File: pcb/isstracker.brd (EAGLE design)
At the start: 68.6 x 54.3 mm, 20 parts, among them IC2 L7805CV, J1 MOTOR_RIGHT, J3 MOTOR_LEFT, J4 DISPLAY, J5 CONTROL, J8 UART, J9 DISTANCE, U1 ARGON, X1 +12V

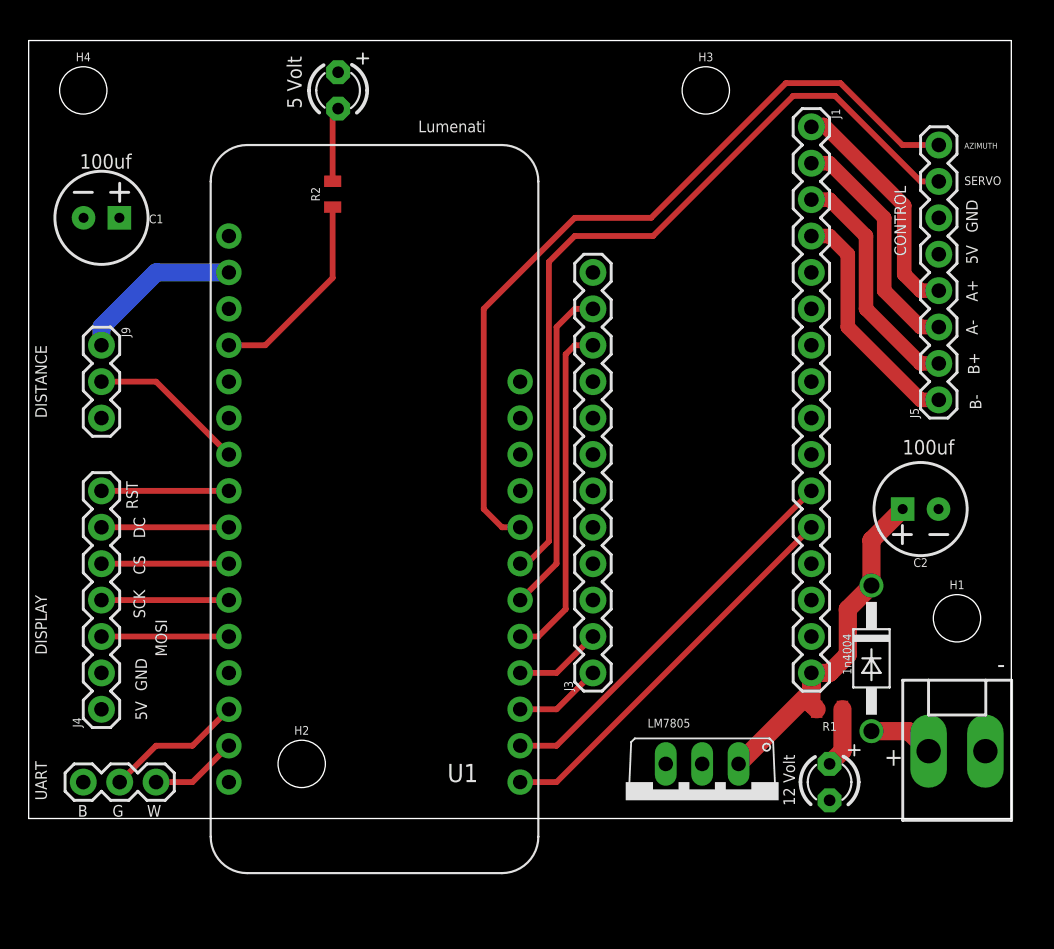
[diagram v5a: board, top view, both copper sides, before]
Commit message: PCB fixups
* Bumped PCB revisions
* Layout changes and some silk screen updates
* No functionality changes
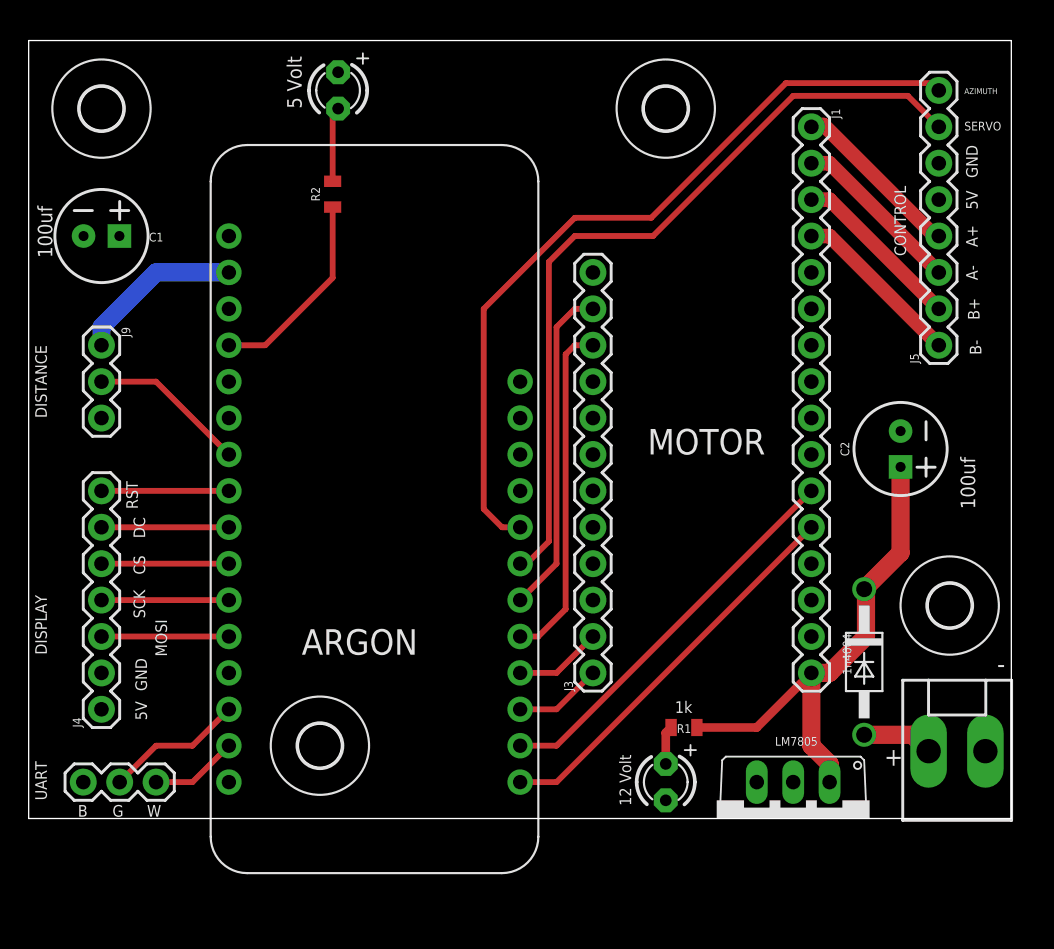
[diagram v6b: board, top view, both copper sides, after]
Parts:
- H1, H2, H3, H4: value STAND-OFF -> MOUNT-HOLE3.0; device SparkFun-Hardware:STAND-OFF -> holes:3,0
- moved H2 46.5 mm to (64.3, 14.9)
- moved H1 45.3 mm to (20.3, 5.08)
- moved LED1 11.4 mm to (44.5, 2.54)
- moved R1 10.2 mm to (45.7, 6.35), turned to 0 degrees
- moved IC2 6.48 mm to (53.3, 0.00)
- moved C2 4.42 mm to (60.8, 25.8), turned to 270 degrees
- moved J5 3.81 mm to (63.5, 33.0)
- moved H3 3.07 mm to (44.5, 49.5)
- moved H4 1.80 mm to (5.08, 49.5)
- moved C1 1.27 mm to (5.08, 40.6)
- moved D1 0.57 mm to (58.3, 10.9)
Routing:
- net +12V: track 26.0 -> 35.5 mm
- net B-: track 16.6 -> 12.0 mm
- net B+: track 16.6 -> 12.0 mm
- net A-: track 16.6 -> 12.0 mm
- net A+: track 16.5 -> 12.2 mm
- net SERVO: track 56.6 -> 55.0 mm
- net AZIMUTH: track 57.1 -> 55.5 mm
- net N$2: track 4.18 -> 2.69 mm
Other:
- board text added: "1k"
- board text added: "ARGON"
- board text added: "MOTOR"
- board text removed: "Lumenati"

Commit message: Fixups
* Add the ability to turn the power to the globe on and off via a MOSFET
* Clean up some of the code
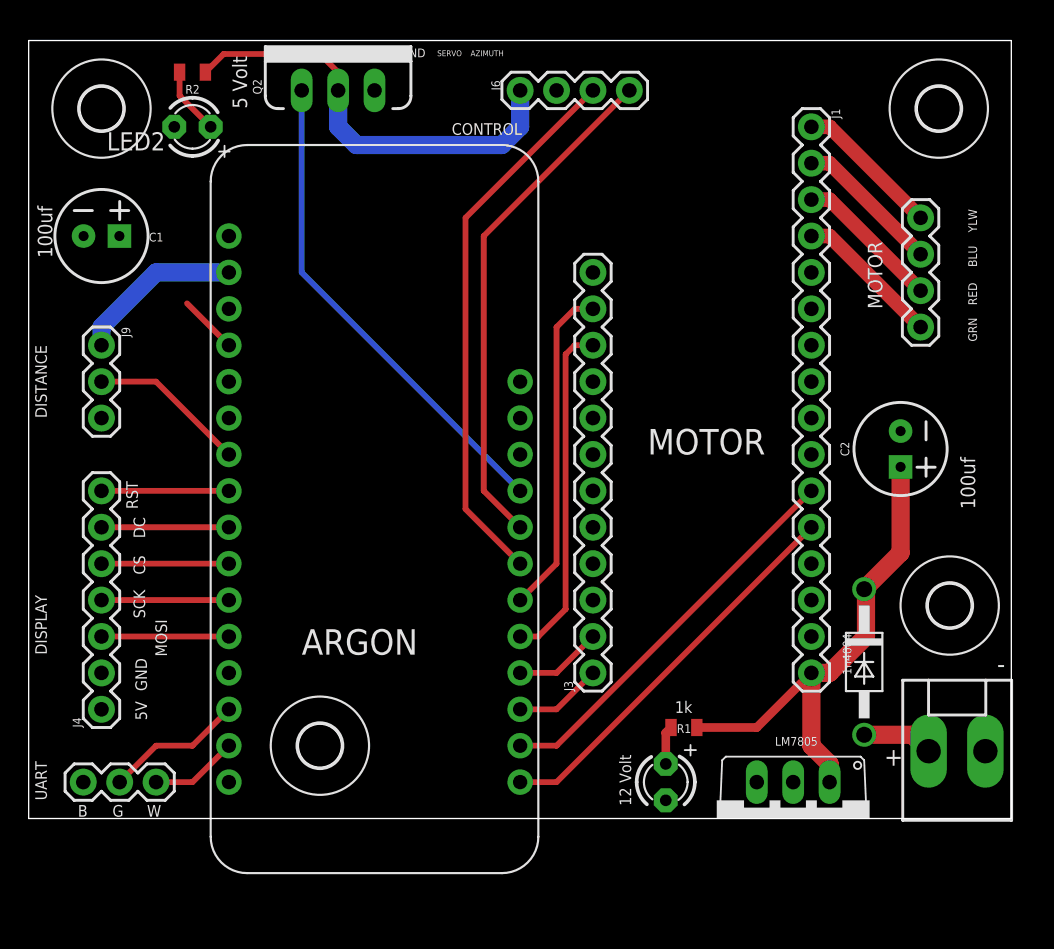
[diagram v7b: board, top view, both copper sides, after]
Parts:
- removed J5: CONTROL, SparkFun-Connectors:1X08
- removed LED3: BLUE, adafruit:LED3MM
- added J2: MOTOR, SparkFun-Connectors:1X04
- added J6: CONTROL, SparkFun-Connectors:1X04
- added LED2: (no value), adafruit:LED3MM
- added Q2: 60V/32A/35mΩ, SparkFun-DiscreteSemi:TO220V
- R2: value 1k -> 0.75
- moved H3 19.0 mm to (63.5, 49.5)
- moved R2 13.0 mm to (11.4, 52.1), turned to 180 degrees
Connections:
- new net D8: Q2.1, U1.25
- new net N$3: J6.1, Q2.2, R2.1
- net +5V: now also Q2.3; no longer J5.5, LED3.A
- net A+: now also J2.4; no longer J5.4
- net A-: now also J2.3; no longer J5.3
- net AZIMUTH: now also J6.4; no longer J5.8
- net B+: now also J2.2; no longer J5.2
- net B-: now also J2.1; no longer J5.1
- net GND: now also J6.2, LED2.K; no longer J5.6, R2.1
- net N$4: now also LED2.A; no longer LED3.K
- net SERVO: now also J6.3; no longer J5.7
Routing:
- net D8: track 0.00 -> 34.3 mm
- net N$3: track 0.00 -> 30.4 mm
- net AZIMUTH: track 55.5 -> 35.7 mm
- net SERVO: track 55.0 -> 38.3 mm
- net GND: track 14.1 -> 4.13 mm
- net A+: track 12.2 -> 10.3 mm
- net B-: track 12.0 -> 10.3 mm
- net B+: track 12.0 -> 10.3 mm
- net A-: track 12.0 -> 10.3 mm
- net N$4: track 5.23 -> 4.71 mm
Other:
- board text added: "BLU"
- board text added: "GRN"
- board text added: "ISS Position Tracker (C) Peter Buelow February, 2021 Version 1.5"
- board text added: "RED"
- board text added: "YLW"
- board text removed: "A+"
- board text removed: "A-"
- board text removed: "B+"
- board text removed: "B-"
- board text removed: "ISS Position Tracker (C) Peter Buelow February, 2021 Version 1.3"

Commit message: Layout tweaks
* Swap pth for smd LED's
* Move globe power pin to new location
* Add support hole for motor board if attached via headers
* Layout fixes for globe with new 4 pin setup
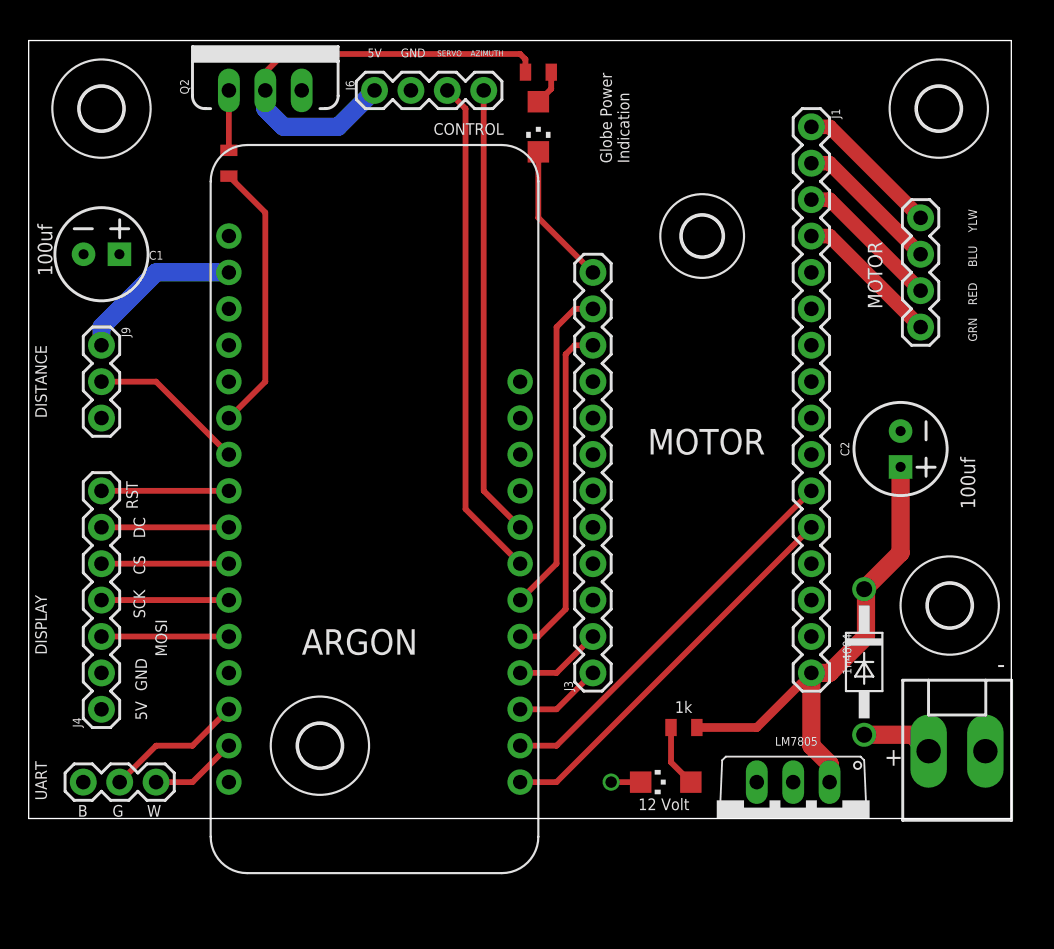
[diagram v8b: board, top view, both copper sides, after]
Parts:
- removed LED2: (no value), adafruit:LED3MM
- added H6: MOUNT-HOLE2.8, holes:2,8
- added LED3: L171L-LPGC, adafruit:CHIPLED_1206
- added R3: 10k, SparkFun-Resistors:0805
- LED1: value RED -> L171L-LPGC; device adafruit:LED3MM -> adafruit:CHIPLED_1206
- R2: value 0.75 -> 1k
- moved LED1 46.6 mm to (35.6, 48.3), turned to 180 degrees
- moved R2 24.1 mm to (35.6, 52.1), turned to 0 degrees
- moved J6 10.2 mm to (24.1, 50.8)
- moved Q2 5.08 mm to (16.5, 50.8)
- moved C1 1.27 mm to (5.08, 39.4)
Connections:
- removed net D8: Q2.1, U1.25
- new net GLOBE_PWR: R3.2, U1.6
- new net N$6: Q2.1, R3.1
- net GND: now also J3.12, LED1.C, LED3.C; no longer LED1.K, LED2.K
- net N$2: now also LED3.A; no longer LED1.A
- net N$4: now also LED1.A; no longer LED2.A
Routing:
- net D8: track 34.3 -> 0.00 mm
- net GLOBE_PWR: track 0.00 -> 19.0 mm
- net GND: track 4.13 -> 12.0 mm, vias 0 -> 1
- net AZIMUTH: track 35.7 -> 31.5 mm
- net N$6: track 0.00 -> 4.18 mm
- net SERVO: track 38.3 -> 35.1 mm
- net N$4: track 4.71 -> 2.43 mm
- net N$2: track 2.69 -> 4.38 mm
- net N$3: track 30.4 -> 31.5 mm
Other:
- board text added: "Globe Power Indication"
- board text added: "ISS Position Tracker (C) Peter Buelow March, 2021 Version 1.6"
- board text removed: "5 Volt"
- board text removed: "ISS Position Tracker (C) Peter Buelow February, 2021 Version 1.5"
